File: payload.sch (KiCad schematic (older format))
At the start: 26 parts

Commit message: Continued syncing with original design.
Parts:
- removed C?: C, ~, symbol C
- removed D? (x2): BI_LED, ~, symbol BI_LED
- removed F? (x6): FUSE, ~, symbol FUSE
- removed K? (x2): CONN_3, symbol CONN_3
- removed P? (x2): CONN_4, symbol CONN_4
- removed Q?: FET_N_GDS, symbol FET_N_GDS
- removed R? (x3): R, ~, symbol R
- removed U? (x2): MIC5014, ~, symbol MIC5014
- removed U? (x2): 74LS74, ~, symbol 74LS74
- added C17: C, ~, symbol C
- added D8, D9: BI_LED, ~, symbol BI_LED
- added F11: 1.1A 24V, ~, symbol FUSE
- added F12: 2.6A 5V, ~, symbol FUSE
- added F13, F9: FUSE, ~, symbol FUSE
- added F14: 1.1A 5V, ~, symbol FUSE
- added F16: 1.85A 24V, ~, symbol FUSE
- added J11, J12, J14, J15, J?: JST-PA-2, ~, symbol CONN_2
- added P1: CONN_2, symbol CONN_2
- added Q5: FET_N_GDS, symbol FET_N_GDS
- added R30, R31, R32: R, ~, symbol R
- added unit 1 of U14
- added unit 1 of U15
- gave numbers to parts that had none: 5
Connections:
- net labels added: +24V
- net labels removed: +BATT, STROBE, SYNC, WING_LIGHT
- wire segments 94 -> 68
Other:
- moved on the sheet: C16, Q6, R29, U15B

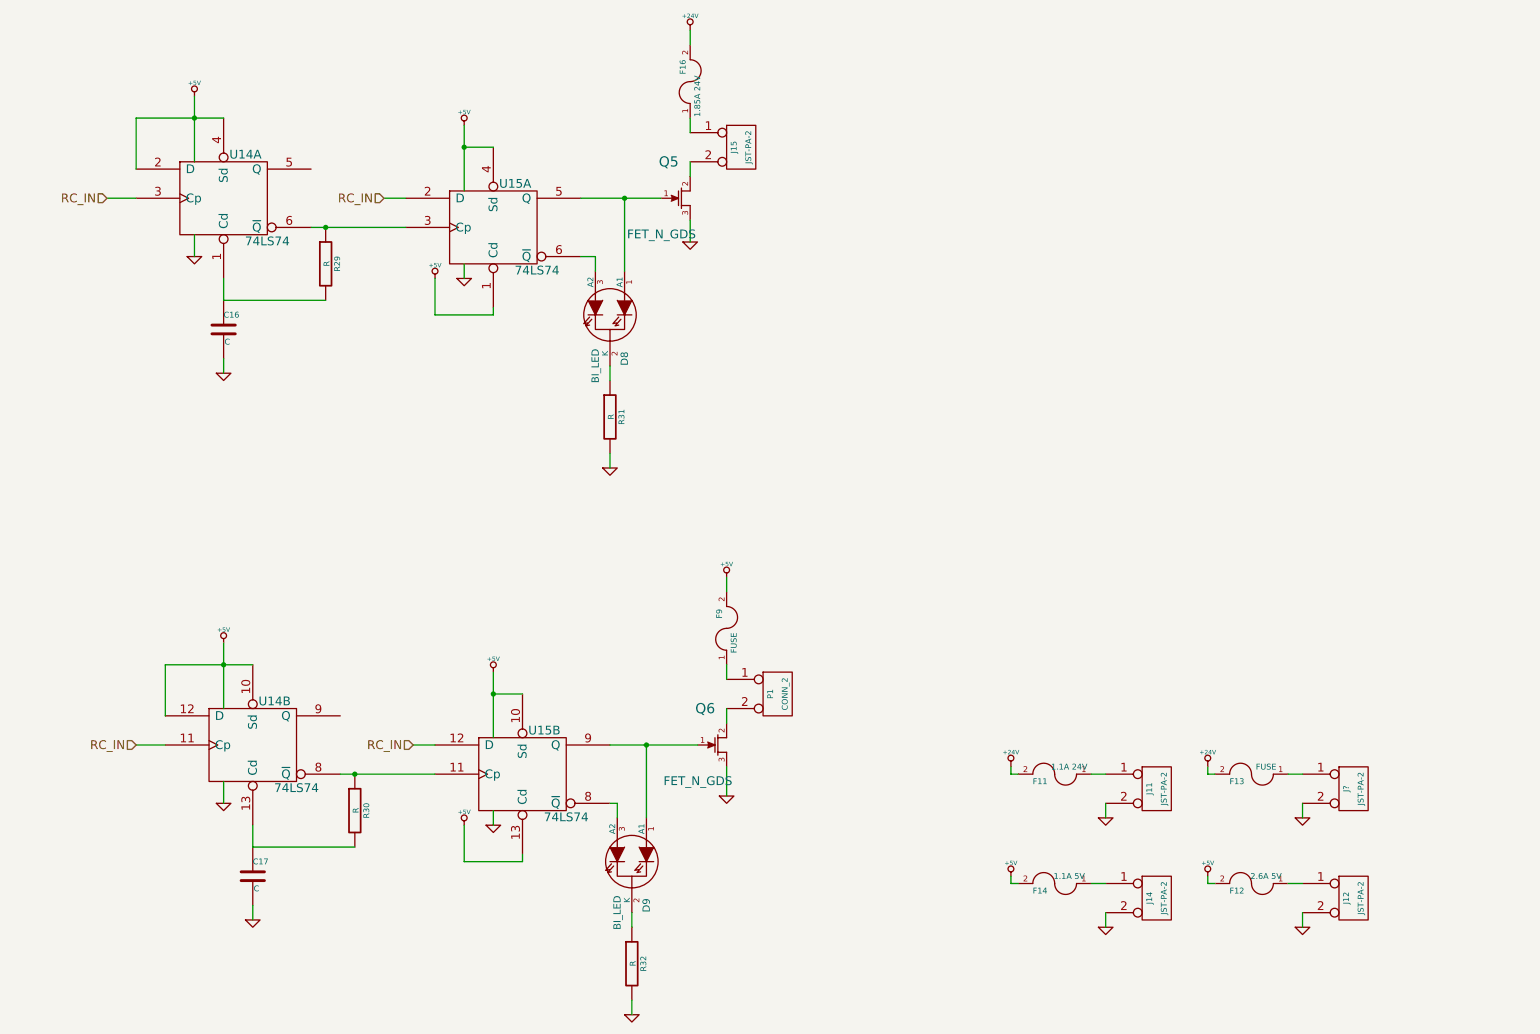
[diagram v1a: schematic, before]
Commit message: Finishing bom integration with schematic.
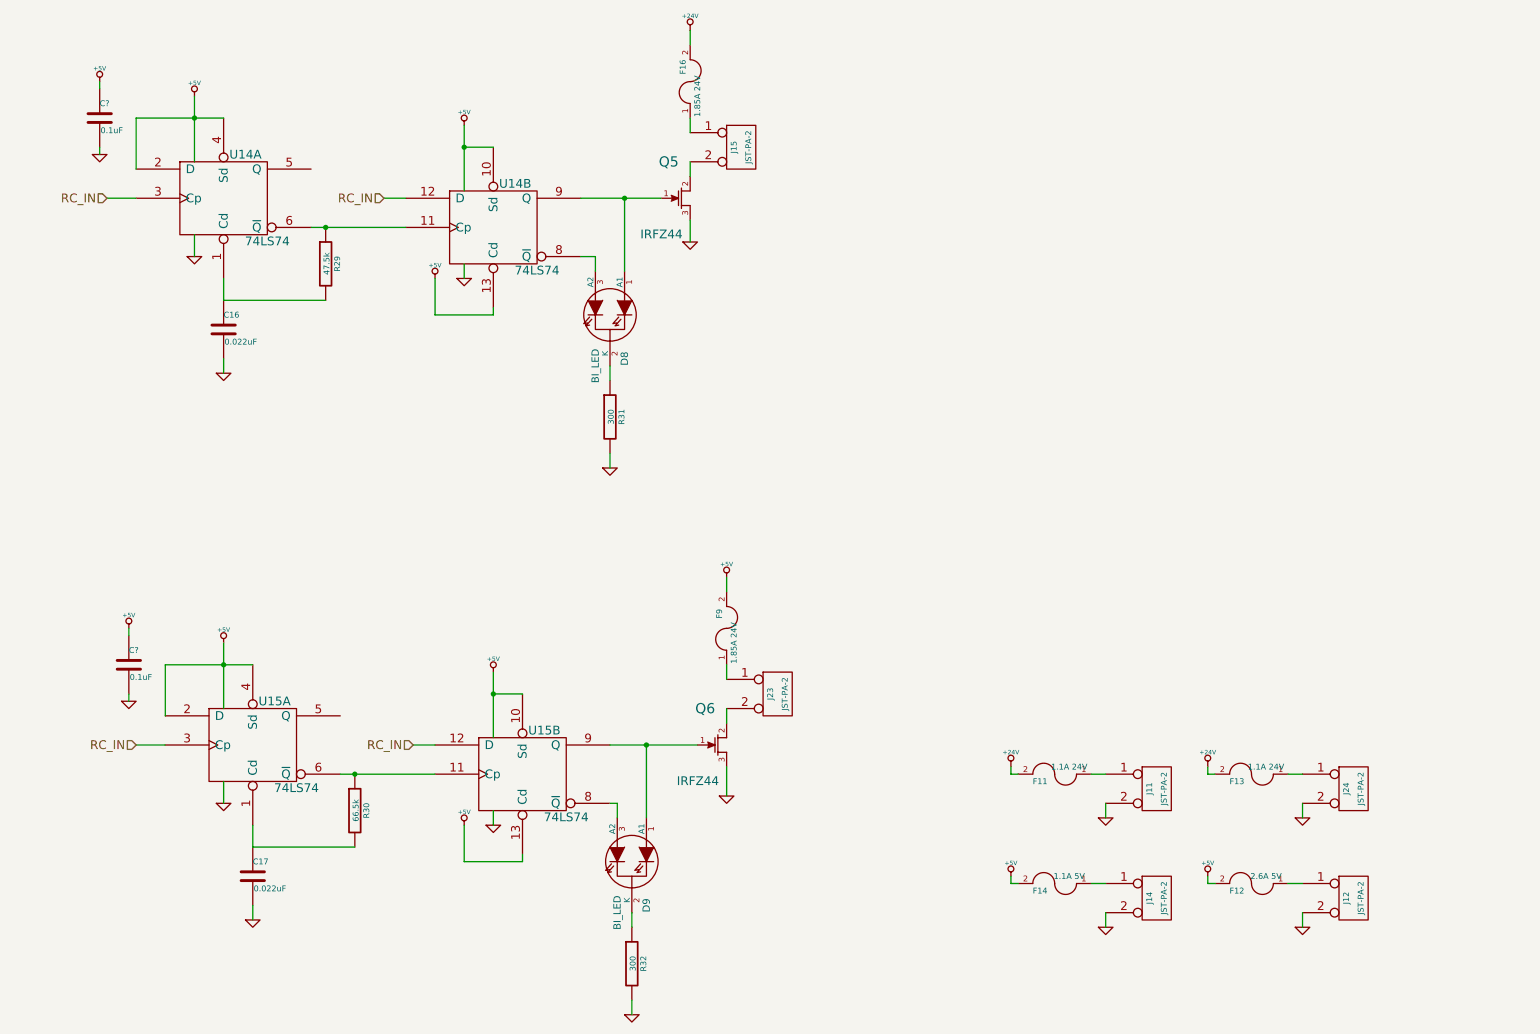
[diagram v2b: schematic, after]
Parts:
- removed P1: CONN_2, symbol CONN_2
- added C? (x2): 0.1uF, SM0805, symbol C
- added J23: JST-PA-2, ~, symbol CONN_2
- C16, C17: value C -> 0.022uF; Digikey (none) -> 490-8308-1-ND
- D8, D9: Digikey (none) -> VLMV3100-GS08CT-ND
- F13: value FUSE -> 1.1A 24V; Digikey (none) -> F2868CT-ND
- F9: value FUSE -> 1.85A 24V; Digikey (none) -> F2871CT-ND
- Q5, Q6: value FET_N_GDS -> IRFZ44; footprint (none) -> ~; Digikey (none) -> IRFZ44STRRPBFCT-ND
- R29: value R -> 47.5k; Digikey (none) -> P47.5KDACT-ND
- R30: value R -> 66.5k; Digikey (none) -> P66.5KDACT-ND
- R31, R32: value R -> 300; Digikey (none) -> P300CCT-ND
- U14, U15: Digikey (none) -> 296-1079-1-ND
- U14: renamed from U15; Digikey (none) -> 296-1079-1-ND
- U15: renamed from U14; Digikey (none) -> 296-1079-1-ND
- gave numbers to parts that had none: 1
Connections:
- net +5V: now also U14.10 (Sd), U14.13 (Cd), U15.2 (D), U15.4 (Sd), C?.1, C?.1; no longer U14.1 (Cd), U14.4 (Sd), U15.10 (Sd), U15.12 (D)
- net GND: now also C?.2, C?.2
- net RC_IN: now also U14.12 (D), U15.3 (Cp); no longer U14.2 (D), U15.11 (Cp)
- net at C17.1, R30.2: now also U15.1 (Cd); no longer U15.13 (Cd)
- net at R30.1, U15.11 (Cp): now also U15.6 (~Q); no longer U15.8 (~Q)
- net at Q6.2 (D): now also J23.2 (PM)
- net at R29.1, U14.6 (~Q): now also U14.11 (Cp); no longer U14.3 (Cp)
- net at F9.1: now also J23.1 (P1)
- net at D8.1 (A1), Q5.1 (G): now also U14.9 (Q); no longer U14.5 (Q)
- net at D8.3 (A2): now also U14.8 (~Q); no longer U14.6 (~Q)
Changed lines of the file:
@@
 LIBS:p_samtec
 LIBS:w_transistor
+LIBS:w_analog
 LIBS:distro-cache
 EELAYER 27 0
@@
 Sheet 8 9
 Title ""
-Date "21 aug 2015"
+Date "22 aug 2015"
 Rev ""
 Comp ""
@@
 $EndDescr
 $Comp
-L 74LS74 U14
-U 2 1 55CD3D59
+L 74LS74 U15
+U 1 1 55CD3D59
 P 2100 5600
-F 0 "U14" H 2250 5900 60  0000 C CNN
+F 0 "U15" H 2250 5900 60  0000 C CNN
 F 1 "74LS74" H 2400 5305 60  0000 C CNN
 F 2 "~" H 2100 5600 60  0000 C CNN
 F 3 "~" H 2100 5600 60  0000 C CNN
-	2    2100 5600
+F 4 "296-1079-1-ND" H 2100 5600 60  0001 C CNN "Digikey"
+	1    2100 5600
 	1    0    0    -1
 $EndComp
@@
 F 2 "~" H 3950 5800 60  0000 C CNN
 F 3 "~" H 3950 5800 60  0000 C CNN
+F 4 "296-1079-1-ND" H 3950 5800 60  0001 C CNN "Digikey"
 	2    3950 5800
 	1    0    0    -1
@@
 P 2100 6500
 F 0 "C17" H 2100 6600 40  0000 L CNN
-F 1 "C" H 2106 6415 40  0000 L CNN
+F 1 "0.022uF" H 2106 6415 40  0000 L CNN
 F 2 "~" H 2138 6350 30  0000 C CNN
 F 3 "~" H 2100 6500 60  0000 C CNN
+F 4 "490-8308-1-ND" H 2100 6500 60  0001 C CNN "Digikey"
 	1    2100 6500
 	1    0    0    -1
@@
 P 2800 6050
 F 0 "R30" V 2880 6050 40  0000 C CNN
-F 1 "R" V 2807 6051 40  0000 C CNN
+F 1 "66.5k" V 2807 6051 40  0000 C CNN
 F 2 "~" V 2730 6050 30  0000 C CNN
 F 3 "~" H 2800 6050 30  0000 C CNN
+F 4 "P66.5KDACT-ND" V 2800 6050 60  0001 C CNN "Digikey"
 	1    2800 6050
 	1    0    0    -1
@@
 P 5300 5600
 F 0 "Q6" H 5203 5850 70  0000 C CNN
-F 1 "FET_N_GDS" H 5153 5353 60  0000 C CNN
-F 2 "" H 5300 5600 60  0000 C CNN
-F 3 "" H 5300 5600 60  0000 C CNN
+F 1 "IRFZ44" H 5153 5353 60  0000 C CNN
+F 2 "~" H 5300 5600 60  0000 C CNN
+F 3 "~" H 5300 5600 60  0000 C CNN
+F 4 "IRFZ44STRRPBFCT-ND" H 5300 5600 60  0001 C CNN "Digikey"
 	1    5300 5600
 	1    0    0    -1
@@
 F 2 "~" H 1900 1850 60  0000 C CNN
 F 3 "~" H 1900 1850 60  0000 C CNN
+F 4 "296-1079-1-ND" H 1900 1850 60  0001 C CNN "Digikey"
 	1    1900 1850
 	1    0    0    -1
 $EndComp
 $Comp
-L 74LS74 U15
-U 1 1 55D6B0B7
+L 74LS74 U14
+U 2 1 55D6B0B7
 P 3750 2050
-F 0 "U15" H 3900 2350 60  0000 C CNN
+F 0 "U14" H 3900 2350 60  0000 C CNN
 F 1 "74LS74" H 4050 1755 60  0000 C CNN
 F 2 "~" H 3750 2050 60  0000 C CNN
 F 3 "~" H 3750 2050 60  0000 C CNN
-	1    3750 2050
+F 4 "296-1079-1-ND" H 3750 2050 60  0001 C CNN "Digikey"
+	2    3750 2050
 	1    0    0    -1
 $EndComp
@@
 P 1900 2750
 F 0 "C16" H 1900 2850 40  0000 L CNN
-F 1 "C" H 1906 2665 40  0000 L CNN
+F 1 "0.022uF" H 1906 2665 40  0000 L CNN
 F 2 "~" H 1938 2600 30  0000 C CNN
 F 3 "~" H 1900 2750 60  0000 C CNN
+F 4 "490-8308-1-ND" H 1900 2750 60  0001 C CNN "Digikey"
 	1    1900 2750
 	1    0    0    -1
@@
 P 2600 2300
 F 0 "R29" V 2680 2300 40  0000 C CNN
-F 1 "R" V 2607 2301 40  0000 C CNN
+F 1 "47.5k" V 2607 2301 40  0000 C CNN
 F 2 "~" V 2530 2300 30  0000 C CNN
 F 3 "~" H 2600 2300 30  0000 C CNN
+F 4 "P47.5KDACT-ND" V 2600 2300 60  0001 C CNN "Digikey"
 	1    2600 2300
 	1    0    0    -1
@@
 P 5050 1850
 F 0 "Q5" H 4953 2100 70  0000 C CNN
-F 1 "FET_N_GDS" H 4903 1603 60  0000 C CNN
-F 2 "" H 5050 1850 60  0000 C CNN
-F 3 "" H 5050 1850 60  0000 C CNN
+F 1 "IRFZ44" H 4903 1603 60  0000 C CNN
+F 2 "~" H 5050 1850 60  0000 C CNN
+F 3 "~" H 5050 1850 60  0000 C CNN
+F 4 "IRFZ44STRRPBFCT-ND" H 5050 1850 60  0001 C CNN "Digikey"
 	1    5050 1850
 	1    0    0    -1
@@
 F 2 "~" H 4700 6400 60  0000 C CNN
 F 3 "~" H 4700 6400 60  0000 C CNN
+F 4 "VLMV3100-GS08CT-ND" H 4700 6400 60  0001 C CNN "Digikey"
 	1    4700 6400
 	0    1    1    0
@@
 F 2 "~" H 4550 2650 60  0000 C CNN
 F 3 "~" H 4550 2650 60  0000 C CNN
+F 4 "VLMV3100-GS08CT-ND" H 4550 2650 60  0001 C CNN "Digikey"
 	1    4550 2650
 	0    1    1    0
@@
 P 4550 3350
 F 0 "R31" V 4630 3350 40  0000 C CNN
-F 1 "R" V 4557 3351 40  0000 C CNN
+F 1 "300" V 4557 3351 40  0000 C CNN
 F 2 "~" V 4480 3350 30  0000 C CNN
 F 3 "~" H 4550 3350 30  0000 C CNN
+F 4 "P300CCT-ND" V 4550 3350 60  0001 C CNN "Digikey"
 	1    4550 3350
 	1    0    0    -1
@@
 P 4700 7100
 F 0 "R32" V 4780 7100 40  0000 C CNN
-F 1 "R" V 4707 7101 40  0000 C CNN
+F 1 "300" V 4707 7101 40  0000 C CNN
 F 2 "~" V 4630 7100 30  0000 C CNN
 F 3 "~" H 4700 7100 30  0000 C CNN
+F 4 "P300CCT-ND" V 4700 7100 60  0001 C CNN "Digikey"
 	1    4700 7100
 	1    0    0    -1
@@
 $EndComp
 $Comp
-L CONN_2 P1
-U 1 1 55D66B4E
-P 5700 5250
-F 0 "P1" V 5650 5250 40  0000 C CNN
-F 1 "CONN_2" V 5750 5250 40  0000 C CNN
-F 2 "" H 5700 5250 60  0000 C CNN
-F 3 "" H 5700 5250 60  0000 C CNN
-	1    5700 5250
-	1    0    0    -1
-$EndComp
-$Comp
 L GND #PWR0103
 U 1 1 55D66B70
@@
 P 5350 4800
 F 0 "F9" H 5450 4850 40  0000 C CNN
-F 1 "FUSE" H 5250 4750 40  0000 C CNN
+F 1 "1.85A 24V" H 5250 4750 40  0000 C CNN
 F 2 "~" H 5350 4800 60  0000 C CNN
 F 3 "~" H 5350 4800 60  0000 C CNN
+F 4 "F2871CT-ND" H 5350 4800 60  0001 C CNN "Digikey"
 	1    5350 4800
 	0    -1   -1   0
@@
 	3750 2600 3750 2650
 Wire Wire Line
-	4350 1850 4900 1850
+	4350 1850 4650 1850
+Wire Wire Line
+	4650 1850 4900 1850
 Wire Wire Line
 	3150 1850 3000 1850
@@
 Connection ~ 2600 2050
 Wire Wire Line
-	2500 2050 3150 2050
+	2500 2050 2600 2050
+Wire Wire Line
+	2600 2050 3150 2050
 Wire Wire Line
 	1900 2550 1900 2400
@@
 Connection ~ 1700 1300
 Wire Wire Line
-	1300 1300 1900 1300
-Wire Wire Line
-	3550 1350 3550 1800
-Wire Wire Line
-	1700 1150 1700 1600
+	1300 1300 1700 1300
+Wire Wire Line
+	1700 1300 1900 1300
+Wire Wire Line
+	3550 1350 3550 1500
+Wire Wire Line
+	3550 1500 3550 1800
+Wire Wire Line
+	1700 1150 1700 1300
+Wire Wire Line
+	1700 1300 1700 1600
 Wire Wire Line
 	3750 6050 3750 6150
@@
 	3950 6350 3950 6400
 Wire Wire Line
-	4550 5600 5150 5600
+	4550 5600 4800 5600
+Wire Wire Line
+	4800 5600 5150 5600
 Wire Wire Line
 	3350 5600 3200 5600
@@
 Connection ~ 2800 5800
 Wire Wire Line
-	2700 5800 3350 5800
+	2700 5800 2800 5800
+Wire Wire Line
+	2800 5800 3350 5800
 Wire Wire Line
 	2100 6300 2100 6150
@@
 Connection ~ 1900 5050
 Wire Wire Line
-	1500 5050 2100 5050
-Wire Wire Line
-	3750 5100 3750 5550
-Wire Wire Line
-	1900 4900 1900 5350
+	1500 5050 1900 5050
+Wire Wire Line
+	1900 5050 2100 5050
+Wire Wire Line
+	3750 5100 3750 5250
+Wire Wire Line
+	3750 5250 3750 5550
+Wire Wire Line
+	1900 4900 1900 5050
+Wire Wire Line
+	1900 5050 1900 5350
 $Comp
 L GND #PWR0107
@@
 P 8950 5800
 F 0 "F13" H 9050 5850 40  0000 C CNN
-F 1 "FUSE" H 8850 5750 40  0000 C CNN
+F 1 "1.1A 24V" H 8850 5750 40  0000 C CNN
 F 2 "~" H 8950 5800 60  0000 C CNN
 F 3 "~" H 8950 5800 60  0000 C CNN
+F 4 "F2868CT-ND" H 8950 5800 60  0001 C CNN "Digikey"
 	1    8950 5800
 	-1   0    0    1
@@
 $EndComp
 $Comp
-L CONN_2 J?
+L CONN_2 J24
 U 1 1 55D6C4F2
 P 9650 5900
-F 0 "J?" V 9600 5900 40  0000 C CNN
+F 0 "J24" V 9600 5900 40  0000 C CNN
 F 1 "JST-PA-2" V 9700 5900 40  0000 C CNN
 F 2 "~" H 9650 5900 60  0000 C CNN
@@
 	1    0    0    -1
 $EndComp
+$Comp
+L C C?
+U 1 1 55D80A93
+P 1050 1300
+F 0 "C?" H 1050 1400 40  0000 L CNN
+F 1 "0.1uF" H 1056 1215 40  0000 L CNN
+F 2 "SM0805" H 1088 1150 30  0001 C CNN
+F 3 "~" H 1050 1300 60  0000 C CNN
+F 4 "399-11163-1-ND" H 1050 1300 60  0001 C CNN "Digikey"
+	1    1050 1300
+	1    0    0    -1
+$EndComp
+$Comp
+L +5V #PWR?
+U 1 1 55D80A99
+P 1050 1050
+F 0 "#PWR?" H 1050 1140 20  0001 C CNN
+F 1 "+5V" H 1050 1140 30  0000 C CNN
+F 2 "" H 1050 1050 60  0000 C CNN
+F 3 "" H 1050 1050 60  0000 C CNN
+	1    1050 1050
+	1    0    0    -1
+$EndComp
+$Comp
+L GND #PWR?
+U 1 1 55D80A9F
+P 1050 1550
+F 0 "#PWR?" H 1050 1550 30  0001 C CNN
+F 1 "GND" H 1050 1480 30  0001 C CNN
+F 2 "" H 1050 1550 60  0000 C CNN
+F 3 "" H 1050 1550 60  0000 C CNN
+	1    1050 1550
+	1    0    0    -1
+$EndComp
+Wire Wire Line
+	1050 1550 1050 1500
+Wire Wire Line
+	1050 1100 1050 1050
+$Comp
+L C C?
+U 1 1 55D80ABD
+P 1250 5050
+F 0 "C?" H 1250 5150 40  0000 L CNN
+F 1 "0.1uF" H 1256 4965 40  0000 L CNN
+F 2 "SM0805" H 1288 4900 30  0001 C CNN
+F 3 "~" H 1250 5050 60  0000 C CNN
+F 4 "399-11163-1-ND" H 1250 5050 60  0001 C CNN "Digikey"
+	1    1250 5050
+	1    0    0    -1
+$EndComp
+$Comp
+L +5V #PWR?
+U 1 1 55D80AC3
+P 1250 4800
+F 0 "#PWR?" H 1250 4890 20  0001 C CNN
+F 1 "+5V" H 1250 4890 30  0000 C CNN
+F 2 "" H 1250 4800 60  0000 C CNN
+F 3 "" H 1250 4800 60  0000 C CNN
+	1    1250 4800
+	1    0    0    -1
+$EndComp
+$Comp
+L GND #PWR?
+U 1 1 55D80AC9
+P 1250 5300
+F 0 "#PWR?" H 1250 5300 30  0001 C CNN
+F 1 "GND" H 1250 5230 30  0001 C CNN
+F 2 "" H 1250 5300 60  0000 C CNN
+F 3 "" H 1250 5300 60  0000 C CNN
+	1    1250 5300
+	1    0    0    -1
+$EndComp
+Wire Wire Line
+	1250 5300 1250 5250
+Wire Wire Line
+	1250 4850 1250 4800
+$Comp
+L CONN_2 J23
+U 1 1 55D8337B
+P 5700 5250
+F 0 "J23" V 5650 5250 40  0000 C CNN
+F 1 "JST-PA-2" V 5750 5250 40  0000 C CNN
+F 2 "~" H 5700 5250 60  0000 C CNN
+F 3 "~" H 5700 5250 60  0000 C CNN
+F 4 "455-2650-1-ND" V 5700 5250 60  0001 C CNN "Digikey"
+	1    5700 5250
+	1    0    0    -1
+$EndComp
